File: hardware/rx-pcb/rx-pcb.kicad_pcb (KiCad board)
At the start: 4 copper layers, 21 parts, among them J1 Conn_01x05_Pin, J2 Conn_01x04_Pin, SW1 SW_SPST, U2 STM32WB05KZV6TR, X1 Q22FA12800025, X2 ABS07-32.768KHZ-1-T

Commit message: RF work start
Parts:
- moved C1 6.12 mm to (142.2, 112.7)
- moved C10 6.12 mm to (146.3, 103.5)
- moved C11 6.12 mm to (150.6, 103.5)
- moved C2 6.12 mm to (148.4, 105.2)
- moved C3 6.12 mm to (148.4, 103.5)
- moved C4 6.12 mm to (152.7, 103.5)
- moved C5 6.12 mm to (151.8, 96.2)
- moved C7 6.12 mm to (146.7, 96.1)
- moved C9 6.12 mm to (144.2, 103.5)
- moved J1 6.12 mm to (155.4, 114.7)
- moved L1 6.12 mm to (146.6, 105.2)
- moved L2 6.12 mm to (144.8, 105.2)
- moved SW1 6.12 mm to (151.3, 114.9)
- moved U2 6.12 mm to (150.0, 100.0)
- moved X1 6.12 mm to (145.8, 96.0)
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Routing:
- net VCC: track 13.8 -> 9.63 mm
- net /rst: track 27.6 -> 24.5 mm
- net /lsei: track 0.00 -> 1.73 mm
- added copper zone on In1.Cu, net GND
- added copper zone on In2.Cu, net GND
- added copper zone on B.Cu, net VCC
- added copper zone on F.Cu, net VCC
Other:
- board outline added: 40 x 40 mm

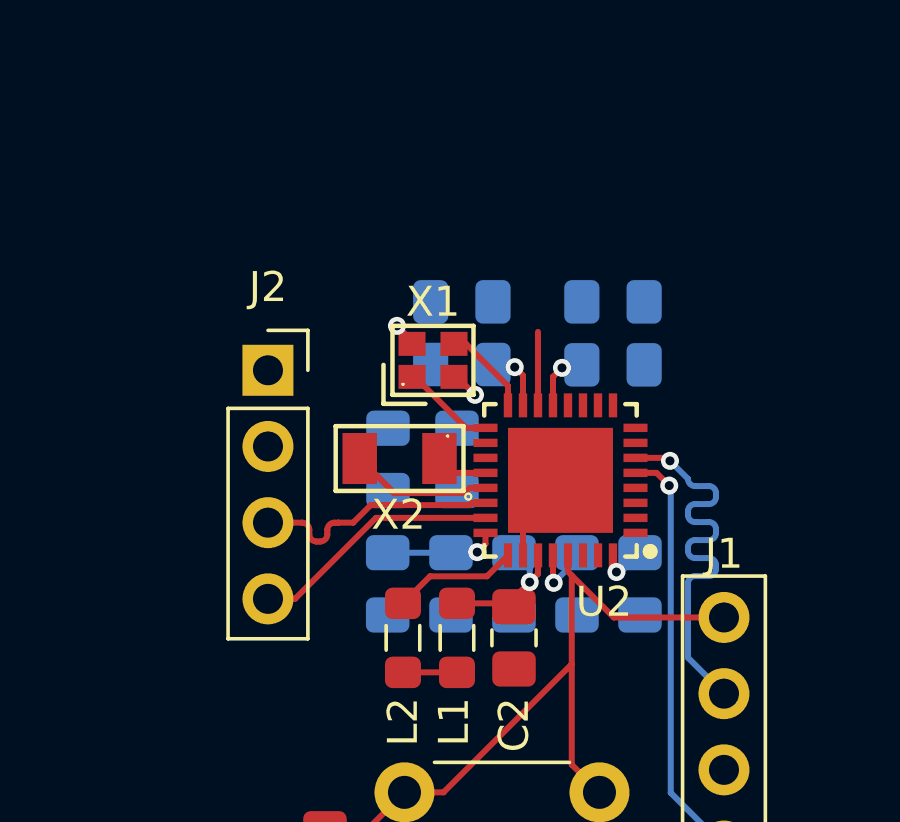
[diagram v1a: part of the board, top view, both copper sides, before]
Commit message: minor board updates. added the MLPF-WB chip for stm impedance matching
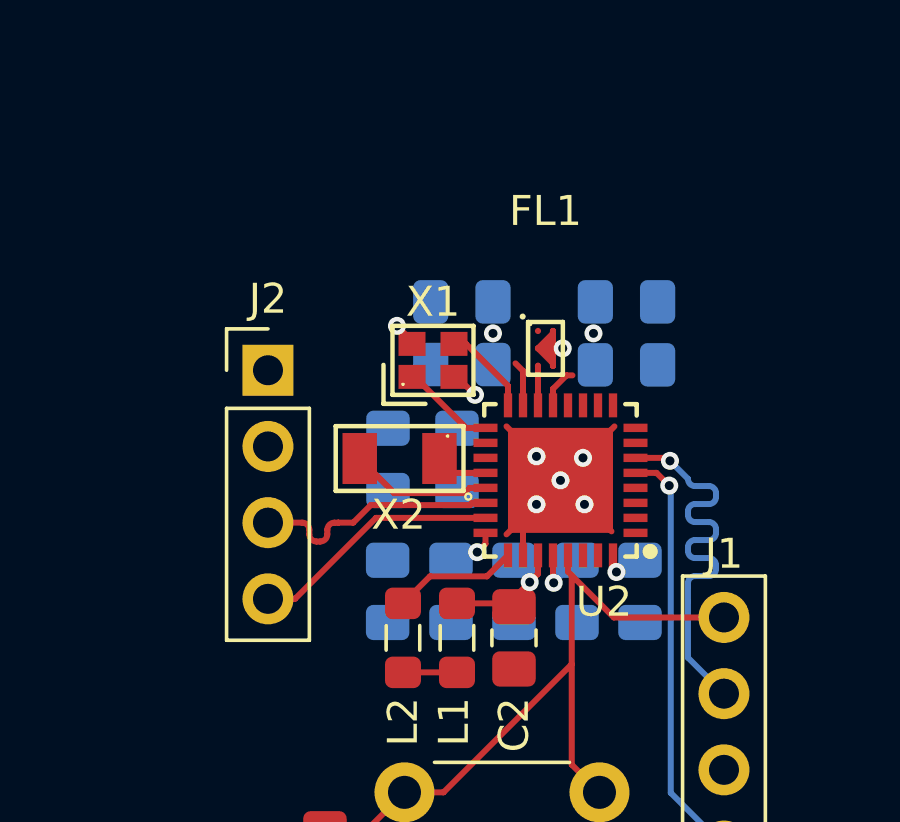
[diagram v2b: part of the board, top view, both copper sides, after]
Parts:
- added FL1: MLPF-WB-01D3, easyeda:BGA-6_L1.6-W1.0-R3-C2-P0.50-TL, F.Cu at (149.5, 95.6)
- J2: footprint Connector_PinSocket_2.54mm:PinSocket_1x04_P2.54mm_Vertical -> Connector_PinHeader_2.54mm:PinHeader_1x04_P2.54mm_Vertical
- moved C5 0.45 mm to (152.2, 96.2)
- moved C6 0.45 mm to (152.2, 94.0)
- moved C10 0.25 mm to (146.3, 103.7)
- moved C11 0.25 mm to (150.6, 103.7)
- moved C3 0.25 mm to (148.4, 103.7)
- moved C4 0.25 mm to (152.7, 103.7)
- moved C9 0.25 mm to (144.2, 103.7)
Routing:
- net GND: track 7.82 -> 21.0 mm, vias 2 -> 8
- net VCC: track 9.63 -> 6.18 mm
- net RF1: track 2.45 -> 1.32 mm

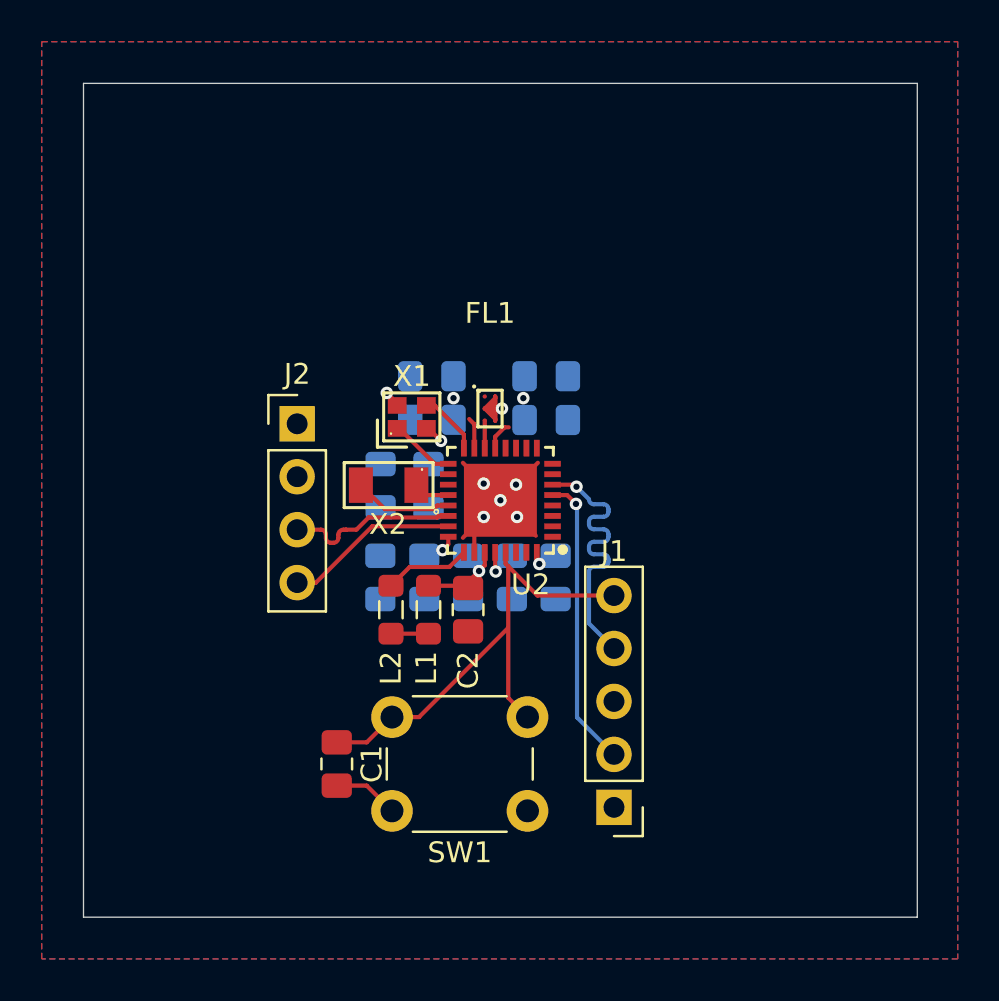
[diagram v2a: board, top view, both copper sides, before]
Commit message: finished initial board. no sensors or power harvesting, but its programmable and bluetooth should work.
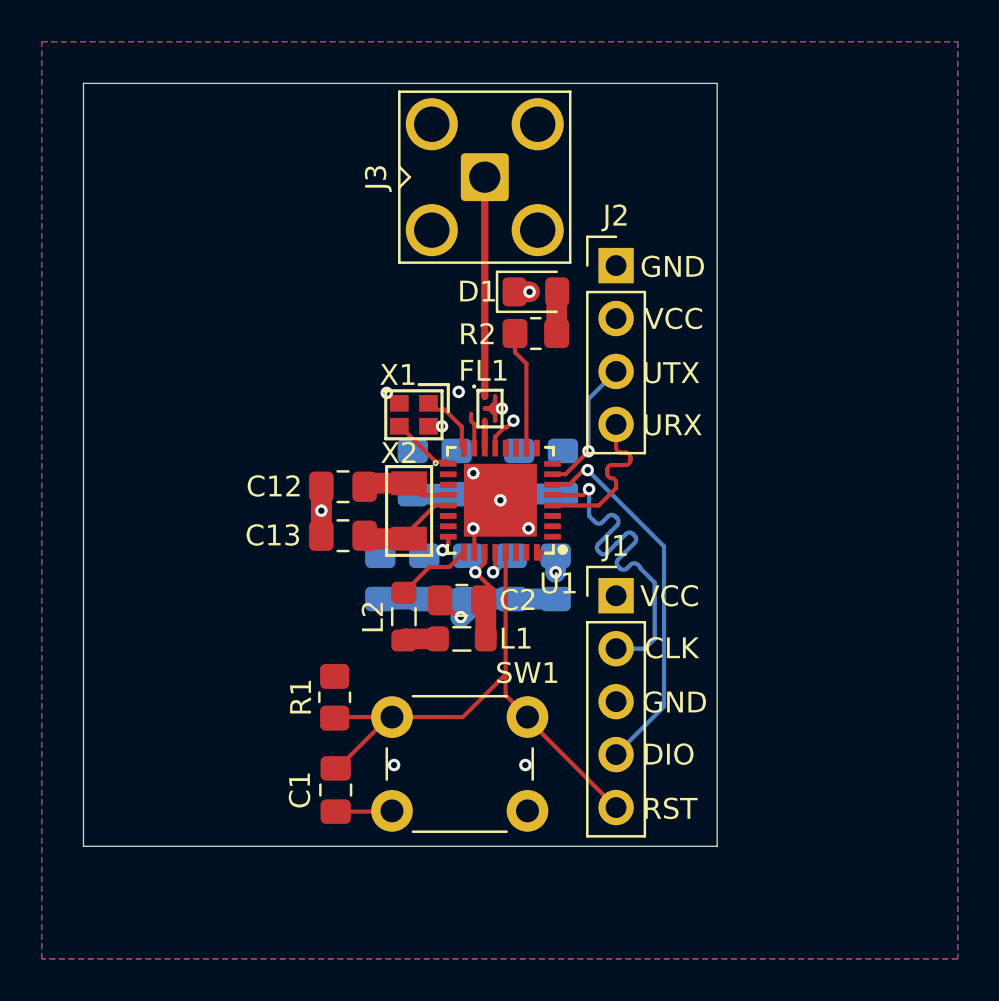
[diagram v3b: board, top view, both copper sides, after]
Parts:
- removed U2: STM32WB05KZV6TR, easyeda:UFQFN-32_L5.0-W5.0-P0.50-TL-EP3.5
- added D1: LED, rx-parts:LED_0805_2012Metric_Pad1.15x1.40mm_HandSolder, F.Cu at (151.7, 90.0)
- added J3: Conn_Coaxial_Small, rx-parts:SMA_Amphenol_901-143_Horizontal, F.Cu at (149.2, 84.5)
- added R1: 100k, rx-parts:R_0805_2012Metric_Pad1.20x1.40mm_HandSolder, F.Cu at (142.1, 109.5)
- added R2: 10k, rx-parts:R_0805_2012Metric_Pad1.20x1.40mm_HandSolder, F.Cu at (151.7, 92.0)
- added U1: STM32WB05KZV6TR, rx-parts:UFQFN-32_L5.0-W5.0-P0.50-TL-EP3.5, F.Cu at (150.0, 100.0)
- C1, C10, C11, C2, C3, C4, C5, C6, C7, C8, C9: footprint Capacitor_SMD:C_0805_2012Metric_Pad1.18x1.45mm_HandSolder -> rx-parts:C_0805_2012Metric_Pad1.18x1.45mm_HandSolder
- C12, C13: footprint Capacitor_SMD:C_0805_2012Metric_Pad1.18x1.45mm_HandSolder -> rx-parts:C_0805_2012Metric_Pad1.18x1.45mm_HandSolder; moved to F.Cu
- FL1: footprint easyeda:BGA-6_L1.6-W1.0-R3-C2-P0.50-TL -> rx-parts:BGA-6_L1.6-W1.0-R3-C2-P0.50-TL
- J1: footprint Connector_PinHeader_2.54mm:PinHeader_1x05_P2.54mm_Vertical -> rx-parts:PinHeader_1x05_P2.54mm_Vertical
- J2: footprint Connector_PinHeader_2.54mm:PinHeader_1x04_P2.54mm_Vertical -> rx-parts:PinHeader_1x04_P2.54mm_Vertical
- L1, L2: footprint Inductor_SMD:L_0805_2012Metric_Pad1.05x1.20mm_HandSolder -> rx-parts:L_0805_2012Metric_Pad1.05x1.20mm_HandSolder
- SW1: footprint Button_Switch_THT:SW_PUSH_6mm -> rx-parts:SW_PUSH_6mm
- X1: footprint easyeda:CRYSTAL-SMD_4P-L2.0-W1.6-BL -> rx-parts:CRYSTAL-SMD_4P-L2.0-W1.6-BL
- X2: footprint easyeda:OSC-SMD_2P-L3.2-W1.5 -> rx-parts:OSC-SMD_2P-L3.2-W1.5
- moved J2 17.1 mm to (155.6, 88.7)
- moved J1 10.2 mm to (155.6, 104.6), turned to 0 degrees
- moved C5 6.88 mm to (145.8, 98.7), turned to -90 degrees
- moved C7 6.78 mm to (153.0, 98.7), turned to -90 degrees
- moved C6 6.31 mm to (147.9, 98.7), turned to -90 degrees
- moved C8 6.24 mm to (150.9, 98.7), turned to -90 degrees
- moved C12 4.10 mm to (142.4, 99.3), turned to 180 degrees
- moved C13 3.00 mm to (142.4, 101.7), turned to 180 degrees
- moved L1 2.13 mm to (148.2, 106.7), turned to 180 degrees
- moved X2 1.58 mm to (145.6, 100.5), turned to -90 degrees
- moved C1 1.25 mm to (142.1, 113.9)
- moved L2 0.70 mm to (145.4, 105.6)
- moved C2 0.54 mm to (148.2, 104.8), turned to 180 degrees
- moved X1 0.14 mm to (145.8, 95.9), turned to 180 degrees
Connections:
- FL1 pad A1: unconnected-(FL1-OUT-PadA1) -> /RF/ANT
- J1 pad 1: 3V3 -> VCC
- J2 pad 2: 3V3 -> VCC
- J2 pad 3: /uart_rx -> /uart_tx
- J2 pad 4: /uart_tx -> /uart_rx
- X1 pad 1: /hsei -> /hseo
- X1 pad 3: /hseo -> /hsei
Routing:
- net /RF/ANT: track 0.00 -> 10.5 mm
- net GND: track 21.0 -> 29.9 mm, vias 8 -> 11
- net Net-(U1-PA9): track 0.00 -> 5.73 mm
- net /swdio: track 14.0 -> 18.1 mm
- net /swclk: track 14.1 -> 18.0 mm
- net /rst: track 24.5 -> 27.2 mm
- net /lsei: track 1.73 -> 4.32 mm
- net Net-(D1-A): track 0.00 -> 2.01 mm
- net /uart_tx: track 8.37 -> 6.56 mm, vias 0 -> 1
- net /hsei: track 3.15 -> 2.55 mm
- net VCC: track 6.18 -> 6.43 mm, vias 4 -> 5
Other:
- board size 40 x 40 mm -> 30.4 x 36.6 mm
- board text added: "CLK"
- board text added: "DIO"
- board text added: "GND"
- board text added: "RST"
- board text added: "URX"
- board text added: "UTX"
- board text added: "VCC"
- board text added: "trace impedance based upon: JLC04161H-7628(Standard/Finished thickness1.59mm±10%)"

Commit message: updated bluetooth section to be in-line with filter datasheet. rearranged LFEX to allow I2C connection.
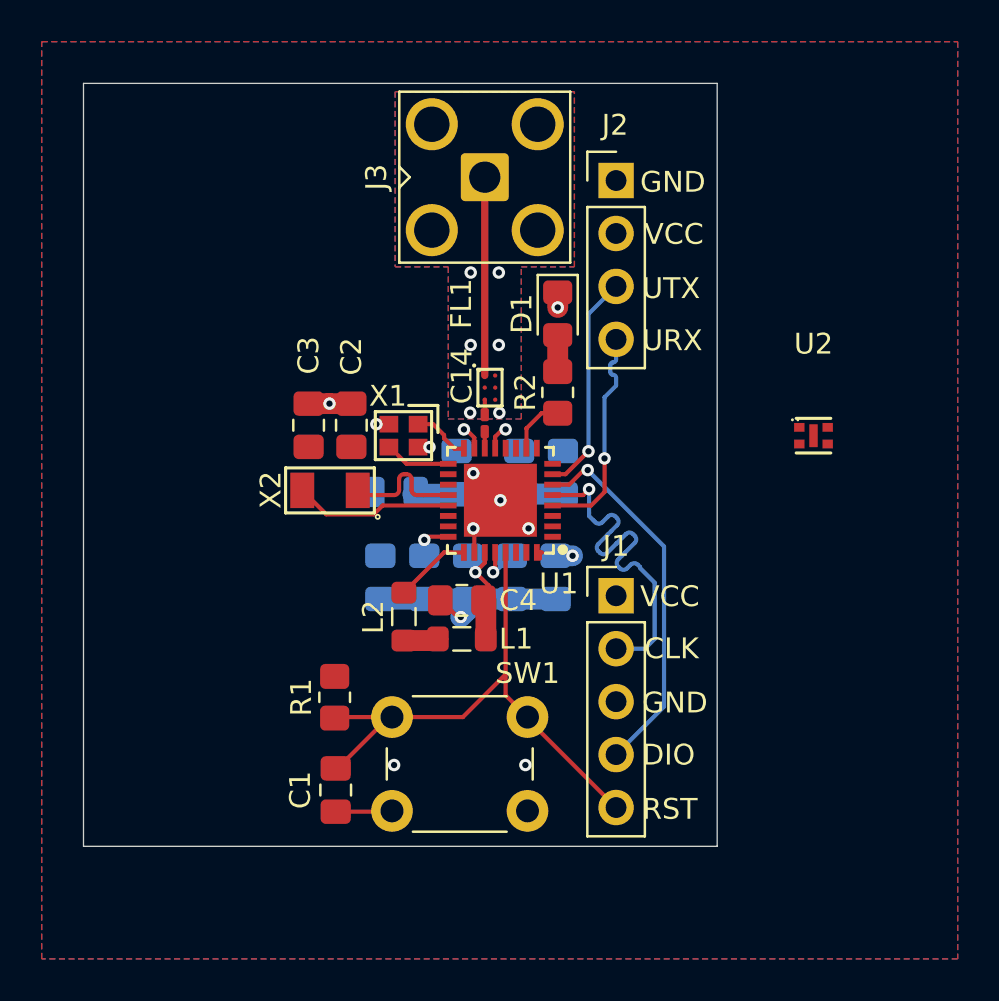
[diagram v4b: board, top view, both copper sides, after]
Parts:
- added C14: 20p, Capacitor_SMD:C_0201_0603Metric_Pad0.64x0.40mm_HandSolder, F.Cu at (149.2, 96.3)
- added U2: STS4L-AD1B-R3, easyeda2kicad:DFN-4_L1.5-W1.5-P0.80-TL-EP, F.Cu at (165.0, 96.9)
- moved C3 5.55 mm to (140.8, 96.4), turned to 90 degrees
- moved J2 4.08 mm to (155.6, 84.7)
- moved X2 3.92 mm to (141.8, 99.5), turned to 180 degrees
- moved R2 3.01 mm to (152.8, 94.8), turned to -90 degrees
- moved C2 2.98 mm to (142.8, 96.4), turned to 90 degrees
- moved D1 1.48 mm to (152.8, 91.0), turned to -90 degrees
- moved C7 1.29 mm to (144.9, 99.6), turned to 0 degrees
- moved X1 1.12 mm to (145.3, 96.9)
- moved FL1 1.00 mm to (149.5, 94.6)
- renumbered C8 to C10, C9 to C11, C10 to C12, C11 to C13, C12 to C2, C13 to C3, C2 to C4, C3 to C5, C4 to C6, C5 to C7, C6 to C8, C7 to C9
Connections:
- FL1 pad A3: RF1 -> Net-(FL1-IN)
- U1 pad 22: unconnected-(U1-PB7-Pad22) -> /i2c_sda
- U1 pad 23: unconnected-(U1-PB6-Pad23) -> /i2c_scl
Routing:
- net GND: track 29.9 -> 25.6 mm, vias 11 -> 16
- net /uart_tx: track 6.56 -> 10.6 mm
- net Net-(U1-PA9): track 5.73 -> 2.75 mm
- net /lseo: track 4.94 -> 7.66 mm
- net /uart_rx: track 8.03 -> 10.6 mm, vias 0 -> 1
- net /lsei: track 4.32 -> 5.99 mm
- net VCC: track 6.43 -> 5.15 mm
- net /RF/ANT: track 10.5 -> 9.52 mm
- net Net-(FL1-IN): track 0.00 -> 0.90 mm
- net RF1: track 1.32 -> 0.79 mm
- added copper zone on B.Cu, net GND
- added copper zone on F.Cu, net GND

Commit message: finished V1 of receiver PCB. No power electronics yet.
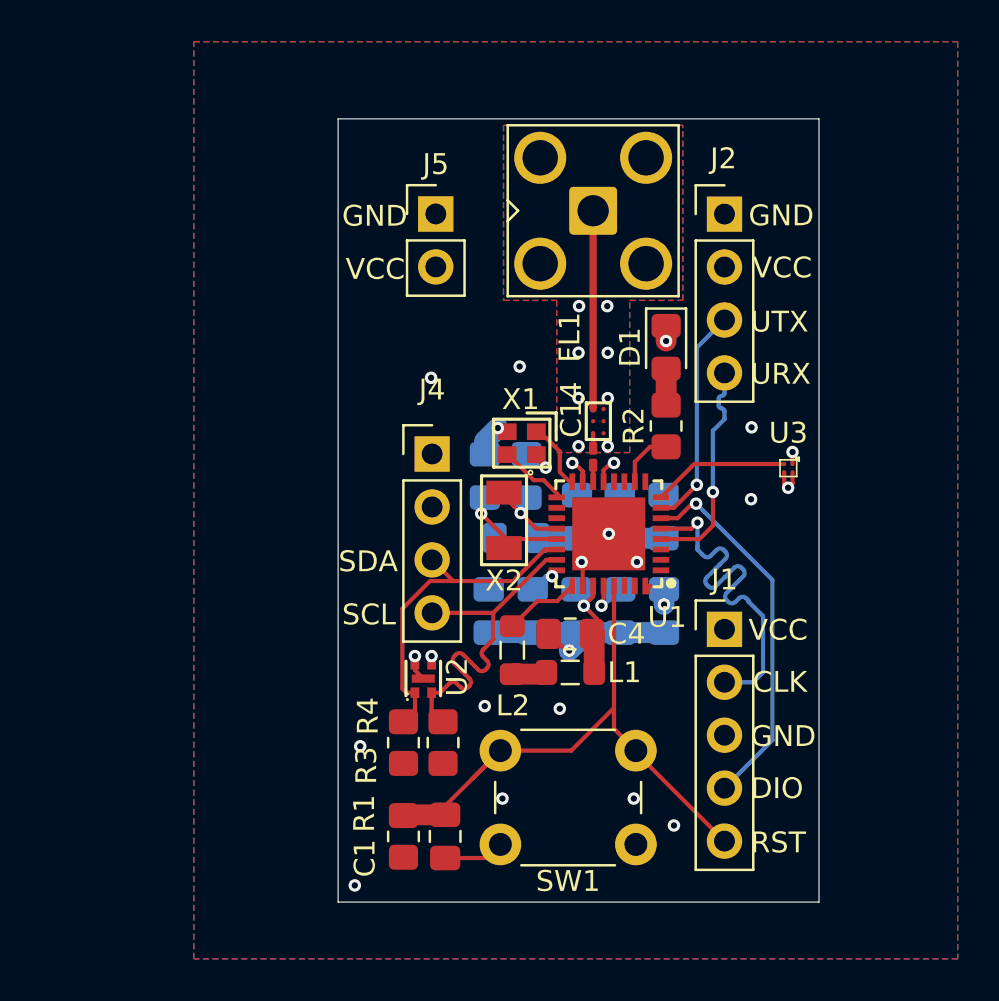
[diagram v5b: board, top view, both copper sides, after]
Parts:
- added J4: Conn_01x04_Pin, rx-parts:PinHeader_1x04_P2.54mm_Vertical, F.Cu at (146.7, 97.8)
- added J5: Conn_01x02_Pin, Connector_PinHeader_2.54mm:PinHeader_1x02_P2.54mm_Vertical, F.Cu at (146.9, 86.3)
- added R3: 100k, rx-parts:R_0805_2012Metric_Pad1.20x1.40mm_HandSolder, F.Cu at (147.2, 111.6)
- added R4: 100k, rx-parts:R_0805_2012Metric_Pad1.20x1.40mm_HandSolder, F.Cu at (145.3, 111.6)
- added U3: LMT70AYFQR, easyeda2kicad:DSBGA-4_L0.8-W0.8-R2-C2-P0.40-BL, F.Cu at (163.8, 98.5)
- C2, C3: moved to B.Cu
- moved U2 22.0 mm to (146.3, 108.5), turned to 90 degrees
- moved C3 8.80 mm to (149.3, 98.8)
- moved C2 8.75 mm to (151.3, 98.8)
- moved X2 8.47 mm to (150.2, 101.0), turned to -90 degrees
- moved R1 7.45 mm to (145.3, 116.1), turned to 90 degrees
- moved C7 6.25 mm to (150.8, 101.8)
- moved C8 6.15 mm to (153.7, 100.8)
- moved C1 5.70 mm to (147.3, 116.1)
- moved X1 5.69 mm to (151.0, 97.3)
- moved C12 5.44 mm to (151.6, 105.3)
- moved C5 5.44 mm to (153.7, 105.3)
- moved C11 5.44 mm to (149.4, 105.3)
- moved C13 5.44 mm to (155.8, 105.3)
- moved C14 5.44 mm to (154.4, 97.9)
- moved C4 5.44 mm to (153.3, 106.4)
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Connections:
- U1 pad 8: unconnected-(U1-PA0-Pad8) -> /TMP_A
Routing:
- net /i2c_scl: track 0.00 -> 17.6 mm
- net /i2c_sda: track 0.00 -> 16.2 mm
- net /TMP_A: track 0.00 -> 6.58 mm
- net /lseo: track 7.66 -> 5.66 mm, vias 0 -> 1
- net /rst: track 27.2 -> 29.0 mm
- net VCC: track 5.15 -> 6.78 mm, vias 5 -> 12
- net /lsei: track 5.99 -> 4.44 mm, vias 0 -> 1
- net /hsei: track 2.20 -> 3.16 mm
- net GND: track 25.6 -> 26.1 mm, vias 16 -> 22
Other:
- board size 30.4 x 36.6 mm -> 23.1 x 37.6 mm
- board text added: "SCL"
- board text added: "SDA"
